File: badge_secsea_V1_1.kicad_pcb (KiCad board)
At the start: 4 copper layers, 74.1 x 130 mm, 132 parts, among them J1 USB_C_Receptacle_USB2.0_14P, J4 AFC07-S24ECA-00, J5 Micro_SD_Card_Det1, Q1 2N7002, Q2 SI1308EDL, Q3 SI2301, SW1 TS-1187A-B-A-B, SW2 K2-1112SW-A4SW-04, SW3 K2-1112SW-A4SW-04, SW4 XDTD-6650, SW5 XDTD-6650, SW6 TS-1187A-B-A-B, SW7 SW_SPDT, U1 RP2040, U2 74HC139, U3 W25Q128JVSIQ, U4 CC1101RGPR, U5 TP4056, U6 TPS63000, U7 LM321, X1 ABM8-272-T3, X2 26MHz

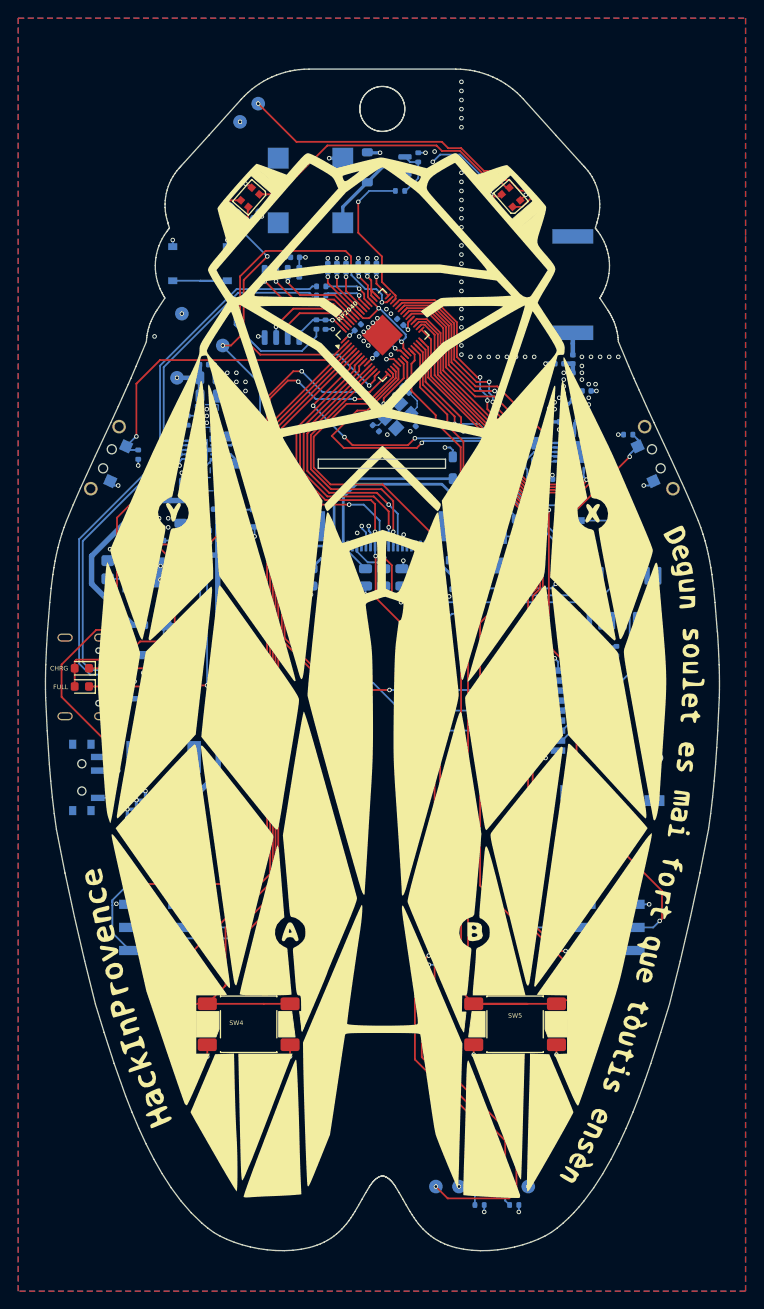
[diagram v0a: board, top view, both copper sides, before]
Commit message: pcb: move some tracks and reduce occupied space using diagonal segments
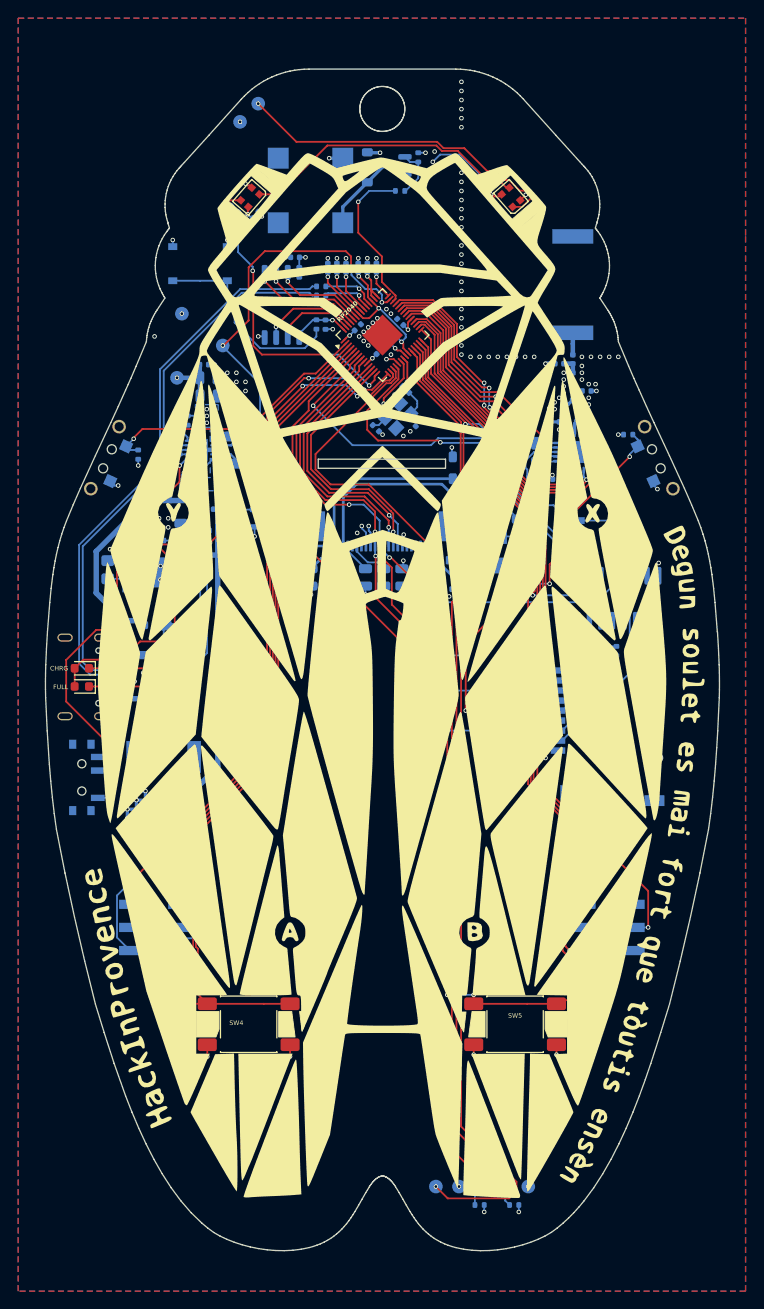
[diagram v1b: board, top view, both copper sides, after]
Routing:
- net SPI0_SCK: track 90.5 -> 72.8 mm, vias 2 -> 5
- net UART0_TX: track 91.3 -> 82.5 mm
- net RUN: track 136.3 -> 128.5 mm, vias 7 -> 5
- net SPI0_RX_MISO: track 73.7 -> 66.1 mm
- net GPIO15_BUTTON_X: track 59.6 -> 52.4 mm
- net I2C0_SCL: track 80.8 -> 74.2 mm
- net GPIO14_BUTTON_B: track 103.5 -> 97.0 mm, vias 1 -> 3
- net Net-(U1-SWD): track 104.5 -> 99.2 mm, vias 3 -> 1
- net Net-(U1-SWCLK): track 103.7 -> 98.6 mm, vias 3 -> 1
- net GPIO18_SPI0_CS_A0: track 45.4 -> 41.9 mm
- net GPIO0_BUTTON_Y: track 33.8 -> 30.5 mm
- net Net-(R3-Pad2): track 25.6 -> 22.5 mm
- net Net-(SW7-B): track 48.0 -> 45.0 mm
- net +3.3V: track 92.9 -> 90.2 mm
- net I2C1_SDA: track 75.5 -> 72.9 mm
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
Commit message: Review with Miaou
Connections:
- SAO0 pad 1: +3.3V -> GND
- SAO0 pad 2: GND -> +3.3V
- SAO0 pad 3: I2C0_SDA -> I2C0_SCL
- SAO0 pad 4: I2C0_SCL -> I2C0_SDA
- SAO1 pad 1: +3.3V -> GND
- SAO1 pad 2: GND -> +3.3V
- SAO1 pad 3: I2C1_SDA -> I2C1_SCL
- SAO1 pad 4: I2C1_SCL -> I2C1_SDA
- SW7 pad : (no net) -> GND
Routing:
- net +3.3V: track 90.2 -> 88.2 mm
- net GND: track 88.2 -> 90.2 mm
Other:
- board text added: "Board V1.2"
- board text removed: "Board V1.1"

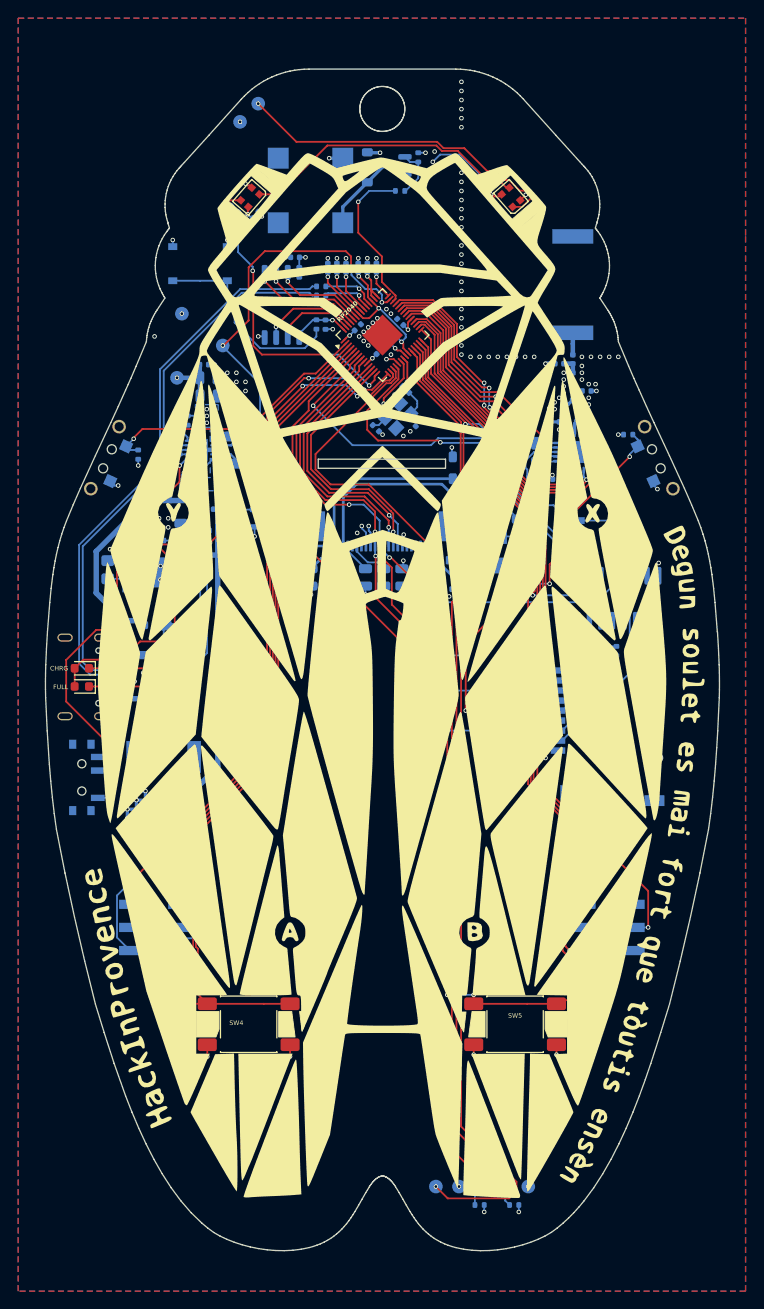
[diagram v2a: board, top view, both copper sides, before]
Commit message: pcb: SAO connector fixed, LED wires on the bottom plane instead of top.
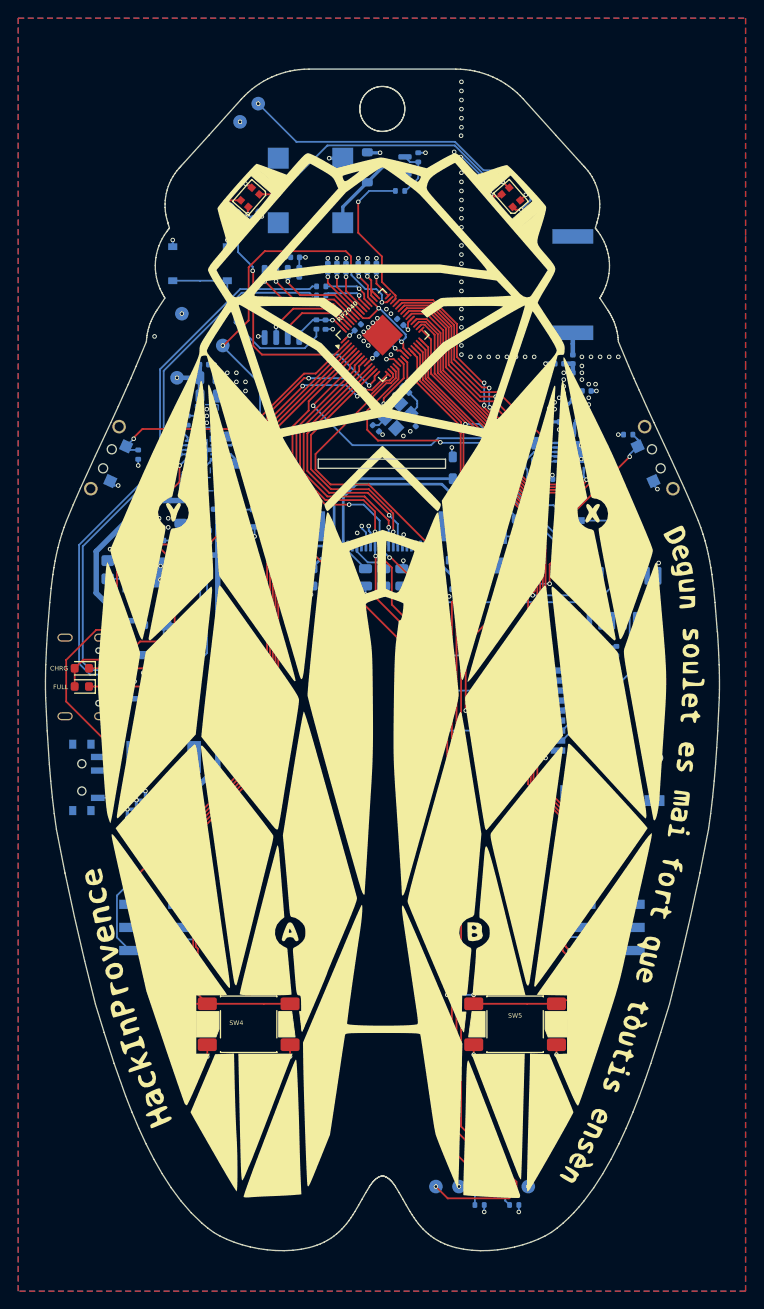
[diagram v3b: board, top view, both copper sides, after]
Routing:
- net GND: track 90.2 -> 78.5 mm, vias 191 -> 196
- net I2C1_SDA: track 72.9 -> 80.5 mm
- net I2C1_SCL: track 80.0 -> 73.2 mm
- net I2C0_SCL: track 74.2 -> 80.5 mm
- net I2C0_SDA: track 78.0 -> 74.0 mm
- net +3.3V: track 88.2 -> 86.9 mm
- net Net-(LED1-DOUT): track 31.7 -> 32.0 mm, vias 0 -> 2
- net Net-(LED2-DOUT): track 37.0 -> 37.3 mm, vias 1 -> 2

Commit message: Schematic backup (before via stitching)
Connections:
- SW7 pad : GND -> (no net)
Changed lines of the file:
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@@
 			)
 		)
-		(attr board_only exclude_from_bom)
+		(attr board_only exclude_from_pos_files exclude_from_bom)
 		(duplicate_pad_numbers_are_jumpers no)
 		(fp_poly
@@
 			)
 		)
+		(property "FT Rotation Offset" "-90"
+			(at 0 0 45)
+			(unlocked yes)
+			(layer "F.Fab")
+			(hide yes)
+			(effects
+				(font
+					(size 1 1)
+					(thickness 0.15)
+				)
+			)
+		)
 		(sheetname "/")
 		(sheetfile "badge_secsea_V1_1.kicad_sch")
@@
 			)
 		)
-		(attr exclude_from_bom)
+		(attr exclude_from_pos_files exclude_from_bom)
 		(duplicate_pad_numbers_are_jumpers no)
 		(fp_circle
@@
 			)
 		)
-		(attr exclude_from_bom)
+		(attr exclude_from_pos_files exclude_from_bom)
 		(duplicate_pad_numbers_are_jumpers no)
 		(fp_circle
@@
 			)
 		)
+		(property "FT Rotation Offset" "-90"
+			(at 0 0 180)
+			(unlocked yes)
+			(layer "B.Fab")
+			(hide yes)
+			(effects
+				(font
+					(size 1 1)
+					(thickness 0.15)
+				)
+				(justify mirror)
+			)
+		)
 		(property ki_fp_filters "*Buzzer*")
 		(sheetname "/")
@@
 			)
 		)
-		(attr exclude_from_bom)
+		(attr exclude_from_pos_files exclude_from_bom)
 		(duplicate_pad_numbers_are_jumpers no)
 		(fp_circle
@@
 			)
 		)
-		(attr exclude_from_bom)
+		(attr exclude_from_pos_files exclude_from_bom)
 		(duplicate_pad_numbers_are_jumpers no)
 		(fp_circle
@@
 			)
 		)
-		(attr exclude_from_bom)
+		(attr exclude_from_pos_files exclude_from_bom)
 		(duplicate_pad_numbers_are_jumpers no)
 		(fp_circle
@@
 			)
 		)
-		(attr exclude_from_bom)
+		(attr exclude_from_pos_files exclude_from_bom)
 		(duplicate_pad_numbers_are_jumpers no)
 		(fp_circle
@@
 			)
 		)
-		(attr exclude_from_bom)
+		(attr exclude_from_pos_files exclude_from_bom)
 		(duplicate_pad_numbers_are_jumpers no)
 		(fp_circle
@@
 			)
 		)
+		(property "FT Rotation Offset" "90"
+			(at 0 0 0)
+			(unlocked yes)
+			(layer "B.Fab")
+			(hide yes)
+			(effects
+				(font
+					(size 1 1)
+					(thickness 0.15)
+				)
+				(justify mirror)
+			)
+		)
 		(property ki_fp_filters "SOT?23*")
 		(sheetname "/")
@@
 			)
 		)
-		(attr exclude_from_bom)
+		(attr exclude_from_pos_files exclude_from_bom)
 		(duplicate_pad_numbers_are_jumpers no)
 		(fp_circle
@@
 			)
 		)
+		(property "FT Rotation Offset" "90"
+			(at 0 0 245.5)
+			(unlocked yes)
+			(layer "B.Fab")
+			(hide yes)
+			(effects
+				(font
+					(size 1 1)
+					(thickness 0.15)
+				)
+				(justify mirror)
+			)
+		)
 		(sheetname "/")
 		(sheetfile "badge_secsea_V1_1.kicad_sch")
@@
 			)
 		)
-		(attr exclude_from_bom)
+		(attr exclude_from_pos_files exclude_from_bom)
 		(duplicate_pad_numbers_are_jumpers no)
 		(fp_circle
@@
 			)
 		)
+		(property "FT Rotation Offset" "90"
+			(at 0 0 114.5)
+			(unlocked yes)
+			(layer "B.Fab")
+			(hide yes)
+			(effects
+				(font
+					(size 1 1)
+					(thickness 0.15)
+				)
+				(justify mirror)
+			)
+		)
 		(sheetname "/")
 		(sheetfile "badge_secsea_V1_1.kicad_sch")
@@
 			)
 		)
-		(attr exclude_from_bom)
+		(attr exclude_from_pos_files exclude_from_bom)
 		(duplicate_pad_numbers_are_jumpers no)
 		(fp_circle
@@
 			)
 		)
+		(property "FT Rotation Offset" "-90"
+			(at 0 0 90)
+			(unlocked yes)
+			(layer "B.Fab")
+			(hide yes)
+			(effects
+				(font
+					(size 1 1)
+					(thickness 0.15)
+				)
+				(justify mirror)
+			)
+		)
 		(sheetname "/")
 		(sheetfile "badge_secsea_V1_1.kicad_sch")
@@
 			(size 1 0.8)
 			(layers "B.Cu" "B.Mask" "B.Paste")
-			(net "GND")
 		)
 		(pad "" smd rect
@@
 			(size 1 0.8)
 			(layers "B.Cu" "B.Mask" "B.Paste")
-			(net "GND")
 		)
 		(pad "" np_thru_hole circle
@@
 			(size 1 0.8)
 			(layers "B.Cu" "B.Mask" "B.Paste")
-			(net "GND")
 		)
 		(pad "" smd rect
@@
 			(size 1 0.8)
 			(layers "B.Cu" "B.Mask" "B.Paste")
-			(net "GND")
 		)
 		(pad "1" smd rect
